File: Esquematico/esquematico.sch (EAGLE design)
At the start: 13 parts

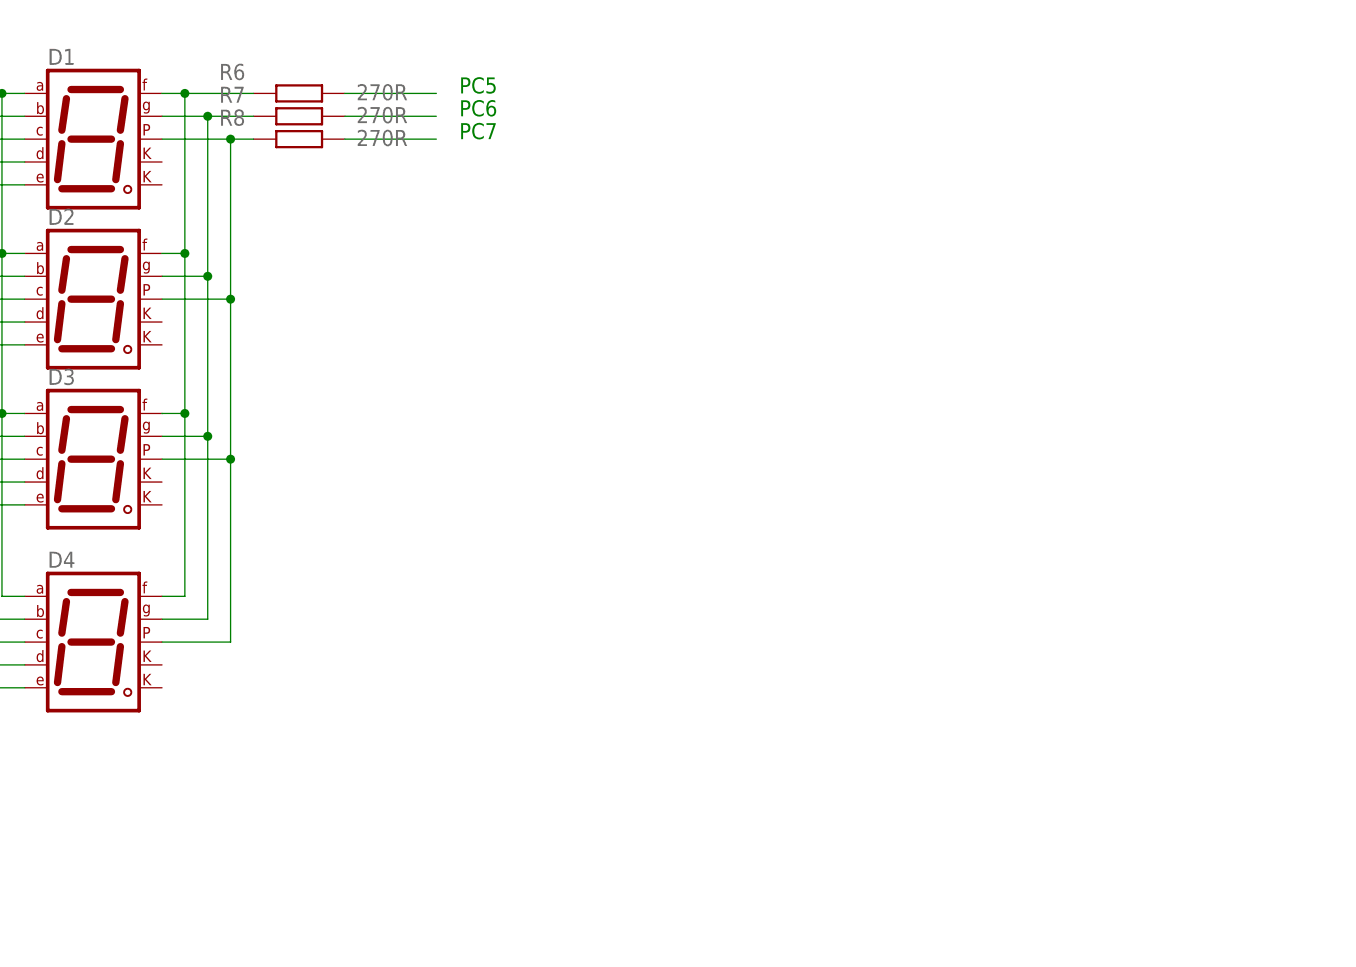
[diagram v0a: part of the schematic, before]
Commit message: Finalização do Esquemático
Transistores adicionados, com resistores, GNDs e conexão com os displays.
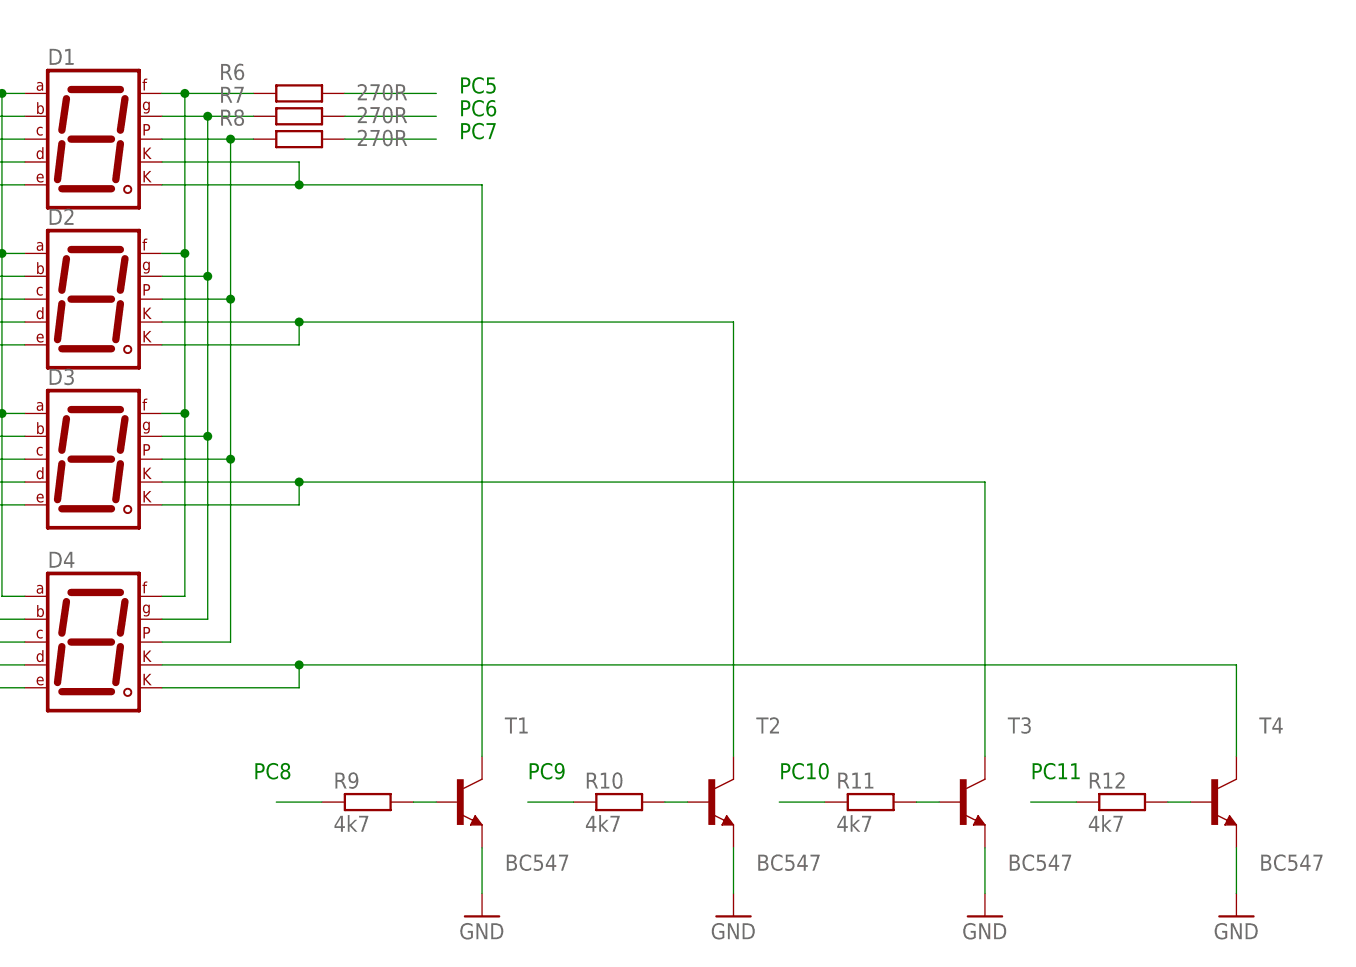
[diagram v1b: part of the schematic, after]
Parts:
- added R10, R11, R12, R9: 4k7, rcl:R-EU_0204/7
- added T1, T2, T3, T4: BC547, transistor:BC547
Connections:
- new net GND: T1.E, T2.E, T3.E, T4.E
- new net N$17: D1.CK1, D1.CK2, T1.C
- new net N$18: R9.2, T1.B
- new net N$19: D2.CK1, D2.CK2, T2.C
- new net N$20: R10.2, T2.B
- new net N$21: D3.CK1, D3.CK2, T3.C
- new net N$22: R11.2, T3.B
- new net N$23: D4.CK1, D4.CK2, T4.C
- new net N$24: R12.2, T4.B
- new net N$25: R12.1
- new net N$26: R11.1
- new net N$27: R10.1
- new net N$28: R9.1
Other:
- note added: "PC10"
- note added: "PC11"
- note added: "PC8"
- note added: "PC9"
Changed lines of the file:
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@@
 <part name="R7" library="rcl" library_urn="urn:adsk.eagle:library:334" deviceset="R-EU_" device="0204/7" package3d_urn="urn:adsk.eagle:package:23498/2" value="270R"/>
 <part name="R8" library="rcl" library_urn="urn:adsk.eagle:library:334" deviceset="R-EU_" device="0204/7" package3d_urn="urn:adsk.eagle:package:23498/2" value="270R"/>
+<part name="T1" library="transistor" library_urn="urn:adsk.eagle:library:402" deviceset="BC547" device="" package3d_urn="urn:adsk.eagle:package:28523/2"/>
+<part name="T2" library="transistor" library_urn="urn:adsk.eagle:library:402" deviceset="BC547" device="" package3d_urn="urn:adsk.eagle:package:28523/2"/>
+<part name="T3" library="transistor" library_urn="urn:adsk.eagle:library:402" deviceset="BC547" device="" package3d_urn="urn:adsk.eagle:package:28523/2"/>
+<part name="T4" library="transistor" library_urn="urn:adsk.eagle:library:402" deviceset="BC547" device="" package3d_urn="urn:adsk.eagle:package:28523/2"/>
+<part name="R9" library="rcl" library_urn="urn:adsk.eagle:library:334" deviceset="R-EU_" device="0204/7" package3d_urn="urn:adsk.eagle:package:23498/2" value="4k7"/>
+<part name="R10" library="rcl" library_urn="urn:adsk.eagle:library:334" deviceset="R-EU_" device="0204/7" package3d_urn="urn:adsk.eagle:package:23498/2" value="4k7"/>
+<part name="R11" library="rcl" library_urn="urn:adsk.eagle:library:334" deviceset="R-EU_" device="0204/7" package3d_urn="urn:adsk.eagle:package:23498/2" value="4k7"/>
+<part name="R12" library="rcl" library_urn="urn:adsk.eagle:library:334" deviceset="R-EU_" device="0204/7" package3d_urn="urn:adsk.eagle:package:23498/2" value="4k7"/>
+<part name="GND1" library="supply1" library_urn="urn:adsk.eagle:library:371" deviceset="GND" device=""/>
+<part name="GND2" library="supply1" library_urn="urn:adsk.eagle:library:371" deviceset="GND" device=""/>
+<part name="GND3" library="supply1" library_urn="urn:adsk.eagle:library:371" deviceset="GND" device=""/>
+<part name="GND4" library="supply1" library_urn="urn:adsk.eagle:library:371" deviceset="GND" device=""/>
 </parts>
 <sheets>
@@
 <text x="111.76" y="25.4" size="1.778" layer="91">PC6</text>
 <text x="111.76" y="22.86" size="1.778" layer="91">PC7</text>
+<text x="88.9" y="-48.26" size="1.778" layer="91">PC8</text>
+<text x="119.38" y="-48.26" size="1.778" layer="91">PC9</text>
+<text x="147.32" y="-48.26" size="1.778" layer="91">PC10</text>
+<text x="175.26" y="-48.26" size="1.778" layer="91">PC11</text>
 </plain>
 <instances>
@@
 <attribute name="NAME" x="85.09" y="24.3586" size="1.778" layer="95"/>
 <attribute name="VALUE" x="100.33" y="22.098" size="1.778" layer="96"/>
+</instance>
+<instance part="T1" gate="G$1" x="111.76" y="-50.8" smashed="yes">
+<attribute name="NAME" x="116.84" y="-43.18" size="1.778" layer="95"/>
+<attribute name="VALUE" x="116.84" y="-58.42" size="1.778" layer="96"/>
+</instance>
+<instance part="T2" gate="G$1" x="139.7" y="-50.8" smashed="yes">
+<attribute name="NAME" x="144.78" y="-43.18" size="1.778" layer="95"/>
+<attribute name="VALUE" x="144.78" y="-58.42" size="1.778" layer="96"/>
+</instance>
+<instance part="T3" gate="G$1" x="167.64" y="-50.8" smashed="yes">
+<attribute name="NAME" x="172.72" y="-43.18" size="1.778" layer="95"/>
+<attribute name="VALUE" x="172.72" y="-58.42" size="1.778" layer="96"/>
+</instance>
+<instance part="T4" gate="G$1" x="195.58" y="-50.8" smashed="yes">
+<attribute name="NAME" x="200.66" y="-43.18" size="1.778" layer="95"/>
+<attribute name="VALUE" x="200.66" y="-58.42" size="1.778" layer="96"/>
+</instance>
+<instance part="R9" gate="G$1" x="101.6" y="-50.8" smashed="yes">
+<attribute name="NAME" x="97.79" y="-49.3014" size="1.778" layer="95"/>
+<attribute name="VALUE" x="97.79" y="-54.102" size="1.778" layer="96"/>
+</instance>
+<instance part="R10" gate="G$1" x="129.54" y="-50.8" smashed="yes">
+<attribute name="NAME" x="125.73" y="-49.3014" size="1.778" layer="95"/>
+<attribute name="VALUE" x="125.73" y="-54.102" size="1.778" layer="96"/>
+</instance>
+<instance part="R11" gate="G$1" x="157.48" y="-50.8" smashed="yes">
+<attribute name="NAME" x="153.67" y="-49.3014" size="1.778" layer="95"/>
+<attribute name="VALUE" x="153.67" y="-54.102" size="1.778" layer="96"/>
+</instance>
+<instance part="R12" gate="G$1" x="185.42" y="-50.8" smashed="yes">
+<attribute name="NAME" x="181.61" y="-49.3014" size="1.778" layer="95"/>
+<attribute name="VALUE" x="181.61" y="-54.102" size="1.778" layer="96"/>
+</instance>
+<instance part="GND1" gate="1" x="114.3" y="-63.5" smashed="yes">
+<attribute name="VALUE" x="111.76" y="-66.04" size="1.778" layer="96"/>
+</instance>
+<instance part="GND2" gate="1" x="142.24" y="-63.5" smashed="yes">
+<attribute name="VALUE" x="139.7" y="-66.04" size="1.778" layer="96"/>
+</instance>
+<instance part="GND3" gate="1" x="170.18" y="-63.5" smashed="yes">
+<attribute name="VALUE" x="167.64" y="-66.04" size="1.778" layer="96"/>
+</instance>
+<instance part="GND4" gate="1" x="198.12" y="-63.5" smashed="yes">
+<attribute name="VALUE" x="195.58" y="-66.04" size="1.778" layer="96"/>
 </instance>
 </instances>
@@
 </segment>
 </net>
+<net name="N$17" class="0">
+<segment>
+<pinref part="D1" gate="G$1" pin="CK2"/>
+<wire x1="78.74" y1="17.78" x2="93.98" y2="17.78" width="0.1524" layer="91"/>
+<pinref part="D1" gate="G$1" pin="CK1"/>
+<wire x1="78.74" y1="20.32" x2="93.98" y2="20.32" width="0.1524" layer="91"/>
+<wire x1="93.98" y1="20.32" x2="93.98" y2="17.78" width="0.1524" layer="91"/>
+<wire x1="93.98" y1="17.78" x2="114.3" y2="17.78" width="0.1524" layer="91"/>
+<junction x="93.98" y="17.78"/>
+<pinref part="T1" gate="G$1" pin="C"/>
+<wire x1="114.3" y1="17.78" x2="114.3" y2="-45.72" width="0.1524" layer="91"/>
+</segment>
+</net>
+<net name="N$19" class="0">
+<segment>
+<pinref part="D2" gate="G$1" pin="CK1"/>
+<wire x1="78.74" y1="2.54" x2="93.98" y2="2.54" width="0.1524" layer="91"/>
+<pinref part="D2" gate="G$1" pin="CK2"/>
+<wire x1="78.74" y1="0" x2="93.98" y2="0" width="0.1524" layer="91"/>
+<wire x1="93.98" y1="0" x2="93.98" y2="2.54" width="0.1524" layer="91"/>
+<pinref part="T2" gate="G$1" pin="C"/>
+<wire x1="93.98" y1="2.54" x2="142.24" y2="2.54" width="0.1524" layer="91"/>
+<wire x1="142.24" y1="2.54" x2="142.24" y2="-45.72" width="0.1524" layer="91"/>
+<junction x="93.98" y="2.54"/>
+</segment>
+</net>
+<net name="N$21" class="0">
+<segment>
+<pinref part="D3" gate="G$1" pin="CK1"/>
+<wire x1="78.74" y1="-15.24" x2="93.98" y2="-15.24" width="0.1524" layer="91"/>
+<pinref part="D3" gate="G$1" pin="CK2"/>
+<wire x1="78.74" y1="-17.78" x2="93.98" y2="-17.78" width="0.1524" layer="91"/>
+<wire x1="93.98" y1="-17.78" x2="93.98" y2="-15.24" width="0.1524" layer="91"/>
+<pinref part="T3" gate="G$1" pin="C"/>
+<wire x1="93.98" y1="-15.24" x2="170.18" y2="-15.24" width="0.1524" layer="91"/>
+<wire x1="170.18" y1="-15.24" x2="170.18" y2="-45.72" width="0.1524" layer="91"/>
+<junction x="93.98" y="-15.24"/>
+</segment>
+</net>
+<net name="N$23" class="0">
+<segment>
+<pinref part="D4" gate="G$1" pin="CK1"/>
+<wire x1="78.74" y1="-35.56" x2="93.98" y2="-35.56" width="0.1524" layer="91"/>
+<wire x1="93.98" y1="-35.56" x2="93.98" y2="-38.1" width="0.1524" layer="91"/>
+<pinref part="D4" gate="G$1" pin="CK2"/>
+<wire x1="93.98" y1="-38.1" x2="78.74" y2="-38.1" width="0.1524" layer="91"/>
+<pinref part="T4" gate="G$1" pin="C"/>
+<wire x1="93.98" y1="-35.56" x2="198.12" y2="-35.56" width="0.1524" layer="91"/>
+<wire x1="198.12" y1="-35.56" x2="198.12" y2="-45.72" width="0.1524" layer="91"/>
+<junction x="93.98" y="-35.56"/>
+</segment>
+</net>
+<net name="N$18" class="0">
+<segment>
+<pinref part="R9" gate="G$1" pin="2"/>
+<pinref part="T1" gate="G$1" pin="B"/>
+<wire x1="106.68" y1="-50.8" x2="109.22" y2="-50.8" width="0.1524" layer="91"/>
+</segment>
+</net>
+<net name="N$20" class="0">
+<segment>
+<pinref part="R10" gate="G$1" pin="2"/>
+<pinref part="T2" gate="G$1" pin="B"/>
+<wire x1="134.62" y1="-50.8" x2="137.16" y2="-50.8" width="0.1524" layer="91"/>
+</segment>
+</net>
+<net name="N$22" class="0">
+<segment>
+<pinref part="R11" gate="G$1" pin="2"/>
+<pinref part="T3" gate="G$1" pin="B"/>
+<wire x1="162.56" y1="-50.8" x2="165.1" y2="-50.8" width="0.1524" layer="91"/>
+</segment>
+</net>
+<net name="N$24" class="0">
+<segment>
+<pinref part="R12" gate="G$1" pin="2"/>
+<pinref part="T4" gate="G$1" pin="B"/>
+<wire x1="190.5" y1="-50.8" x2="193.04" y2="-50.8" width="0.1524" layer="91"/>
+</segment>
+</net>
+<net name="GND" class="0">
+<segment>
+<pinref part="T1" gate="G$1" pin="E"/>
+<pinref part="GND1" gate="1" pin="GND"/>
+<wire x1="114.3" y1="-55.88" x2="114.3" y2="-60.96" width="0.1524" layer="91"/>
+</segment>
+<segment>
+<pinref part="T3" gate="G$1" pin="E"/>
+<pinref part="GND3" gate="1" pin="GND"/>
+<wire x1="170.18" y1="-55.88" x2="170.18" y2="-60.96" width="0.1524" layer="91"/>
+</segment>
+<segment>
+<pinref part="T4" gate="G$1" pin="E"/>
+<pinref part="GND4" gate="1" pin="GND"/>
+<wire x1="198.12" y1="-55.88" x2="198.12" y2="-60.96" width="0.1524" layer="91"/>
+</segment>
+<segment>
+<pinref part="T2" gate="G$1" pin="E"/>
+<wire x1="142.24" y1="-55.88" x2="142.24" y2="-60.96" width="0.1524" layer="91"/>
+<pinref part="GND2" gate="1" pin="GND"/>
+</segment>
+</net>
+<net name="N$25" class="0">
+<segment>
+<pinref part="R12" gate="G$1" pin="1"/>
+<wire x1="180.34" y1="-50.8" x2="175.26" y2="-50.8" width="0.1524" layer="91"/>
+</segment>
+</net>
+<net name="N$26" class="0">
+<segment>
+<pinref part="R11" gate="G$1" pin="1"/>
+<wire x1="152.4" y1="-50.8" x2="147.32" y2="-50.8" width="0.1524" layer="91"/>
+</segment>
+</net>
+<net name="N$27" class="0">
+<segment>
+<pinref part="R10" gate="G$1" pin="1"/>
+<wire x1="124.46" y1="-50.8" x2="119.38" y2="-50.8" width="0.1524" layer="91"/>
+</segment>
+</net>
+<net name="N$28" class="0">
+<segment>
+<pinref part="R9" gate="G$1" pin="1"/>
+<wire x1="96.52" y1="-50.8" x2="91.44" y2="-50.8" width="0.1524" layer="91"/>
+</segment>
+</net>

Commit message: GND
Faltava o GND conectado ao ARM para estabelecer a referência.
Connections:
- net GND: now also U$1.GND1
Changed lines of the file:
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@@
 <part name="GND3" library="supply1" library_urn="urn:adsk.eagle:library:371" deviceset="GND" device=""/>
 <part name="GND4" library="supply1" library_urn="urn:adsk.eagle:library:371" deviceset="GND" device=""/>
+<part name="GND5" library="supply1" library_urn="urn:adsk.eagle:library:371" deviceset="GND" device=""/>
 </parts>
 <sheets>
@@
 <attribute name="VALUE" x="195.58" y="-66.04" size="1.778" layer="96"/>
 </instance>
+<instance part="GND5" gate="1" x="53.34" y="63.5" smashed="yes">
+<attribute name="VALUE" x="50.8" y="60.96" size="1.778" layer="96"/>
+</instance>
 </instances>
 <busses>
@@
 <pinref part="GND2" gate="1" pin="GND"/>
 </segment>
-</net>
+<segment>
+<pinref part="U$1" gate="G$1" pin="GND1"/>
+<wire x1="58.42" y1="68.58" x2="53.34" y2="68.58" width="0.1524" layer="91"/>
+<pinref part="GND5" gate="1" pin="GND"/>
+<wire x1="53.34" y1="68.58" x2="53.34" y2="66.04" width="0.1524" layer="91"/>
+</segment>
+</net>
